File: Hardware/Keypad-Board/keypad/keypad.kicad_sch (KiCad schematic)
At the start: 0 parts

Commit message: PCB design complete, ready for fitment testing
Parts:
- added H1, H2, H3, H4: MountingHole, MountingHole:MountingHole_2.7mm_M2.5, symbol Mechanical:MountingHole
- added J1: Conn_01x07, Connector_JST:JST_XH_B7B-XH-A_1x07_P2.50mm_Vertical, symbol Connector_Generic:Conn_01x07
- added SW1, SW10, SW11, SW12, SW2, SW3, SW4, SW5, SW6, SW7, SW8, SW9: SW_Push_45deg, Button_Switch_Keyboard:SW_Cherry_MX_1.00u_PCB, symbol Switch:SW_Push_45deg
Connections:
- new net Col_0: J1.3 (Pin_3), SW1.1, SW4.1, SW7.1, SW8.1
- new net Col_1: J1.2 (Pin_2), SW10.1, SW2.1, SW5.1, SW9.1
- new net Col_2: J1.1 (Pin_1), SW11.1, SW12.1, SW3.1, SW6.1
- new net Row_0: J1.4 (Pin_4), SW1.2, SW2.2, SW3.2
- new net Row_1: J1.5 (Pin_5), SW4.2, SW5.2, SW6.2
- new net Row_2: J1.6 (Pin_6), SW11.2, SW7.2, SW9.2
- new net Row_3: J1.7 (Pin_7), SW10.2, SW12.2, SW8.2
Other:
- note added: "'0'"
- note added: "'1'"
- note added: "'2'"
- note added: "'3'"
- note added: "'4'"
- note added: "'5'"
- note added: "'6'"
- note added: "'7'"
- note added: "'8'"
- note added: "'9'"
- note added: "'START'"
- note added: "'STOP'"

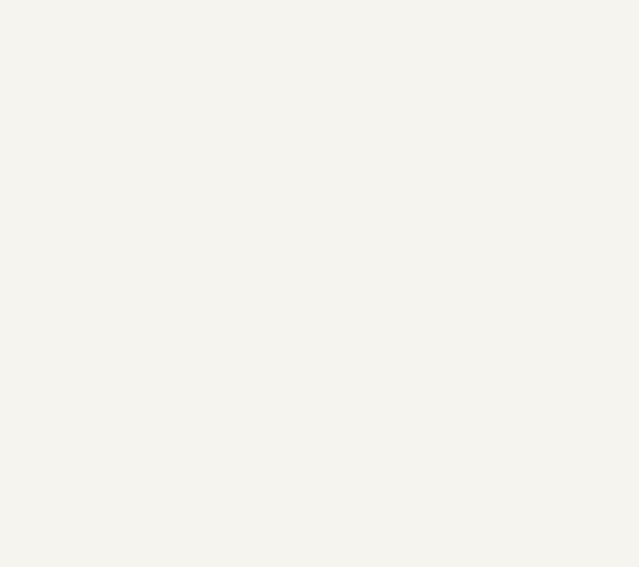
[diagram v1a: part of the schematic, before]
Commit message: Add daughter board for power and reset, send to production
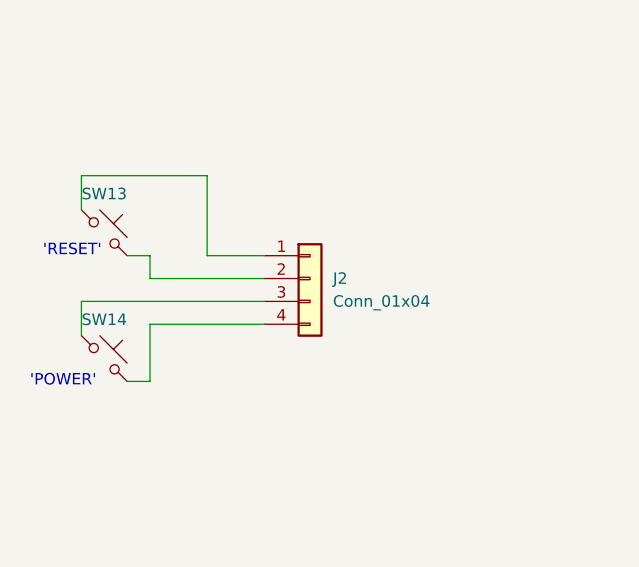
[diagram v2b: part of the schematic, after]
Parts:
- added J2: Conn_01x04, Connector_JST:JST_XH_B4B-XH-A_1x04_P2.50mm_Vertical, symbol Connector_Generic:Conn_01x04
- added SW13, SW14: SW_Push_45deg, Button_Switch_Keyboard:SW_Cherry_MX_1.00u_PCB, symbol Switch:SW_Push_45deg
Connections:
- new net: J2.1 (Pin_1), SW13.1
- new net: J2.2 (Pin_2), SW13.2
- new net: J2.3 (Pin_3), SW14.1
- new net: J2.4 (Pin_4), SW14.2
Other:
- note added: "'POWER'"
- note added: "'RESET'"
